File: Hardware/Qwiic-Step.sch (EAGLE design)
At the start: 69 parts, among them J1 PTH, J2 Qwiic Right Angle, J3 5.5x2.1mm Barrel, J4 Qwiic Right Angle, J5 ISP, U1 A4988ALT1, U2 ATMEGA328P_TQFP, U44 OPA344, Y1 16MHz

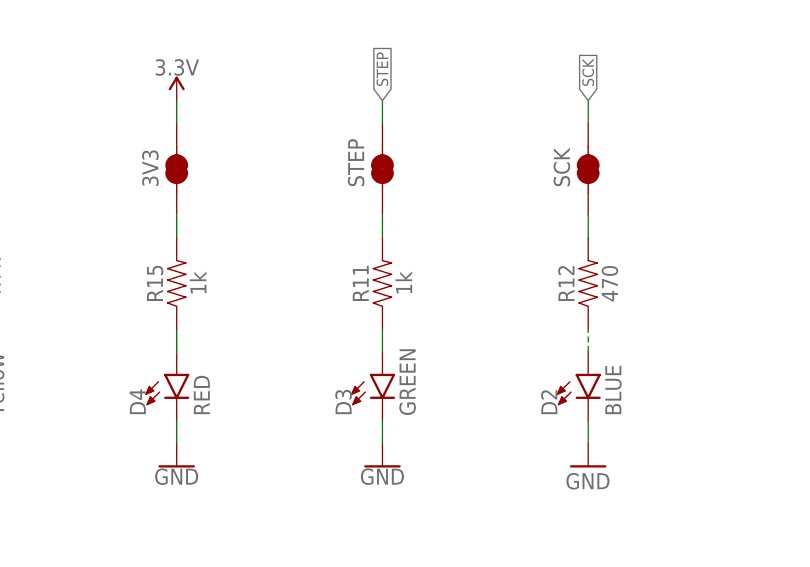
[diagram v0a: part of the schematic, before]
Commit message: Change resistor values on VIN and STEP LEDs.
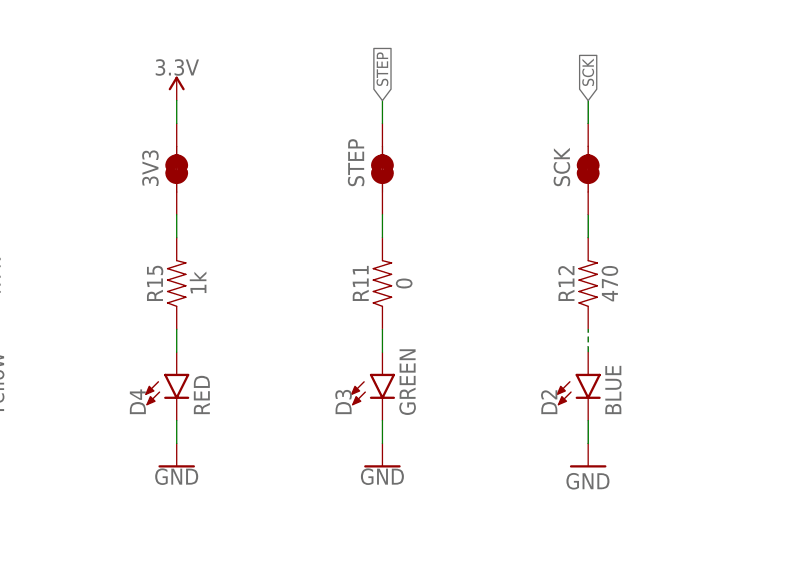
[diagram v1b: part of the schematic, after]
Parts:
- R11: value 1k -> 0; device SparkFun-Resistors:1KOHM-0603-1/10W-1% -> SparkFun-Resistors:0OHM-0603-1/10W
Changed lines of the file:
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@@
 <?xml version="1.0" encoding="utf-8"?>
 <!DOCTYPE eagle SYSTEM "eagle.dtd">
-<eagle version="9.4.2">
+<eagle version="9.5.2">
 <drawing>
 <settings>
@@
 <part name="JP10" library="SparkFun-Hardware" deviceset="STAND-OFF" device=""/>
 <part name="GND5" library="SparkFun-PowerSymbols" deviceset="GND" device=""/>
-<part name="R11" library="SparkFun-Resistors" deviceset="1KOHM" device="-0603-1/10W-1%" value="1k"/>
+<part name="R11" library="SparkFun-Resistors" deviceset="0OHM" device="-0603-1/10W" value="0"/>
 <part name="D3" library="SparkFun-LED" deviceset="LED-GREEN" device="0603" value="GREEN"/>
 <part name="GND6" library="SparkFun-PowerSymbols" deviceset="GND" device=""/>

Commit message: Increasing yellow LED resistor to 10k to limit brightness
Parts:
- R1: value 4.7k -> 10k; device SparkFun-Resistors:4.7KOHM-0603-1/10W-1% -> SparkFun-Resistors:10KOHM-0603-1/10W-1%
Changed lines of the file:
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@@
 <part name="SUPPLY11" library="SparkFun-PowerSymbols" deviceset="3.3V" device=""/>
 <part name="J4" library="SparkFun-Connectors" deviceset="I2C_STANDARD" device="QWIIC" value="Qwiic Right Angle"/>
-<part name="R1" library="SparkFun-Resistors" deviceset="4.7KOHM" device="-0603-1/10W-1%" value="4.7k"/>
+<part name="R1" library="SparkFun-Resistors" deviceset="10KOHM" device="-0603-1/10W-1%" value="10k"/>
 <part name="VIN" library="SparkFun-Jumpers" deviceset="JUMPER-SMT_2_NC_TRACE" device="_SILK" package3d_urn="urn:adsk.eagle:package:39281/1" value="JUMPER-SMT_2_NC_TRACE_SILK"/>
 <part name="SUPPLY13" library="SparkFun-PowerSymbols" deviceset="3.3V" device=""/>

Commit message: Change CUR_REF_PWM RC filter to 100k/1uF.
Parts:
- C2: value 10nF -> 1.0uF; device SparkFun-Capacitors:10NF-0603-50V-10% -> SparkFun-Capacitors:1.0UF-0603-16V-10%
- R3: value 33k -> 100k; device SparkFun-Resistors:33KOHM-0603-1/10W-1% -> SparkFun-Resistors:100KOHM-0603-1/10W-1%
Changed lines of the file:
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@@
 <part name="3V3" library="SparkFun-Jumpers" deviceset="JUMPER-SMT_2_NC_TRACE" device="_SILK" package3d_urn="urn:adsk.eagle:package:39281/1" value="JUMPER-SMT_2_NC_TRACE_SILK"/>
 <part name="D2" library="SparkFun-LED" deviceset="LED-BLUE" device="0603" value="BLUE"/>
-<part name="R3" library="SparkFun-Resistors" deviceset="33KOHM" device="-0603-1/10W-1%" value="33k"/>
-<part name="C2" library="SparkFun-Capacitors" deviceset="10NF" device="-0603-50V-10%" value="10nF"/>
+<part name="R3" library="SparkFun-Resistors" deviceset="100KOHM" device="-0603-1/10W-1%" value="100k"/>
+<part name="C2" library="SparkFun-Capacitors" deviceset="1.0UF" device="-0603-16V-10%" value="1.0uF"/>
 <part name="ADR" library="SparkFun-Jumpers" deviceset="JUMPER-SMT_2_NO" device="_SILK" package3d_urn="urn:adsk.eagle:package:39279/1" value="ADR"/>
 <part name="D5" library="SparkFun-LED" deviceset="LED-YELLOW" device="0603" value="Yellow"/>

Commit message: Change PWM filter to use X7R rated cap.
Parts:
- C2: device SparkFun-Capacitors:1.0UF-0603-16V-10% -> SparkFun-Capacitors:1.0UF-0603-16V-10%-X7R
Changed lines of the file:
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@@
 <part name="D2" library="SparkFun-LED" deviceset="LED-BLUE" device="0603" value="BLUE"/>
 <part name="R3" library="SparkFun-Resistors" deviceset="100KOHM" device="-0603-1/10W-1%" value="100k"/>
-<part name="C2" library="SparkFun-Capacitors" deviceset="1.0UF" device="-0603-16V-10%" value="1.0uF"/>
+<part name="C2" library="SparkFun-Capacitors" deviceset="1.0UF" device="-0603-16V-10%-X7R" value="1.0uF"/>
 <part name="ADR" library="SparkFun-Jumpers" deviceset="JUMPER-SMT_2_NO" device="_SILK" package3d_urn="urn:adsk.eagle:package:39279/1" value="ADR"/>
 <part name="D5" library="SparkFun-LED" deviceset="LED-YELLOW" device="0603" value="Yellow"/>
